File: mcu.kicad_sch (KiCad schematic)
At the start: 23 parts, among them J3 Conn_01x05, J4 Conn_01x05, U13 STM32F405RGTx, Y1 12MHz

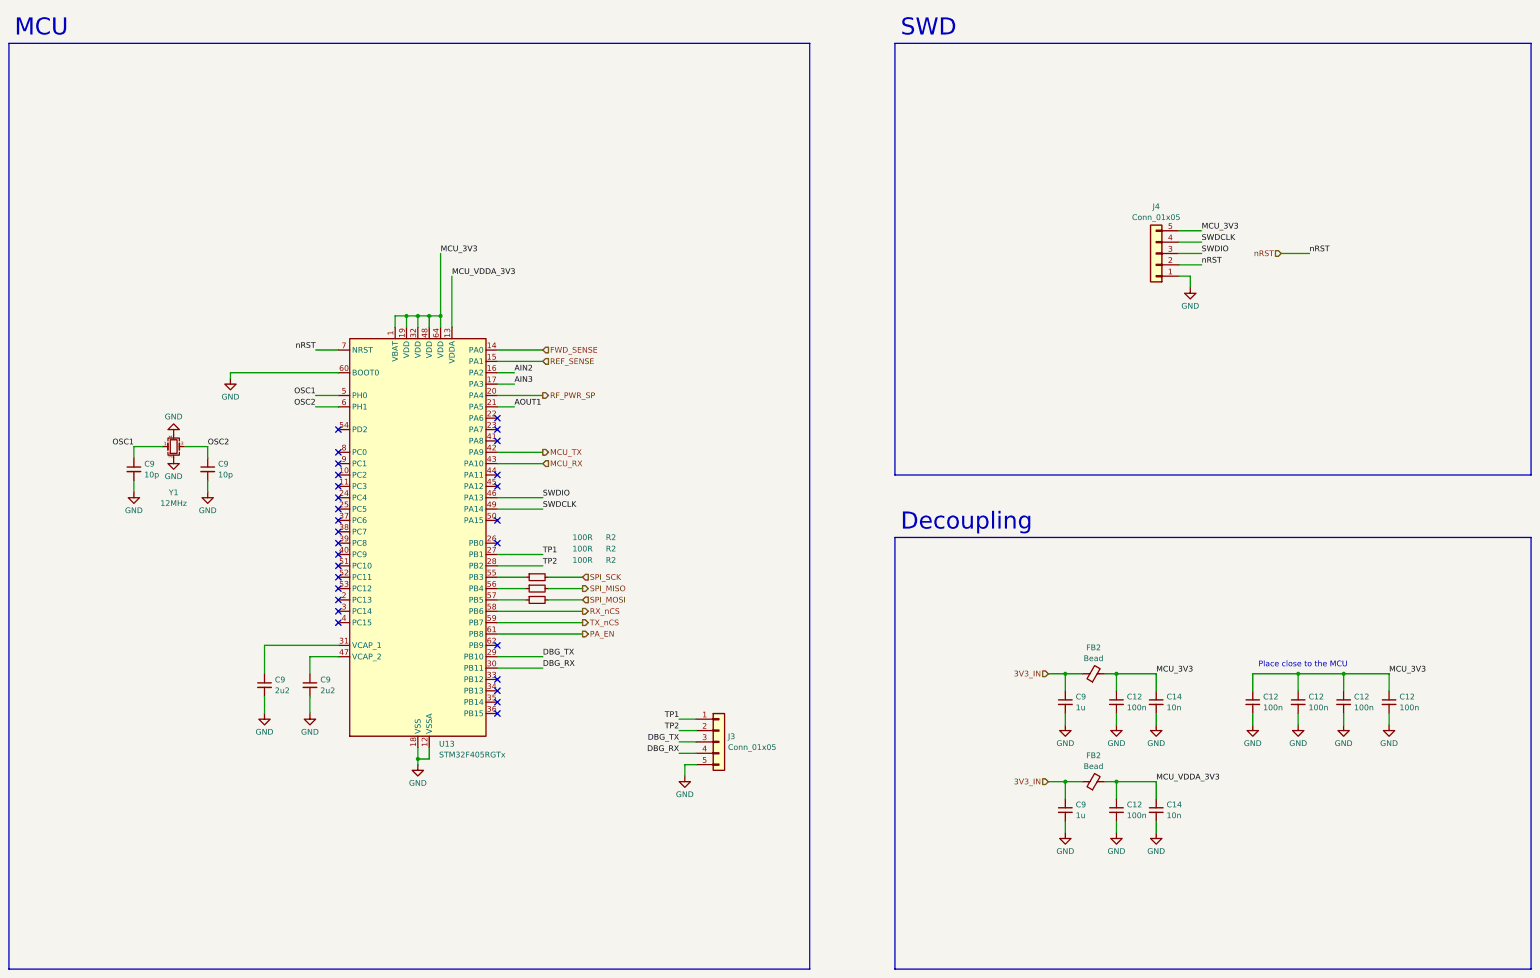
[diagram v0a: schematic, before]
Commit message: significant updates
- supply for the detector block changed from 3.3V to 5V
- minor bugfixes
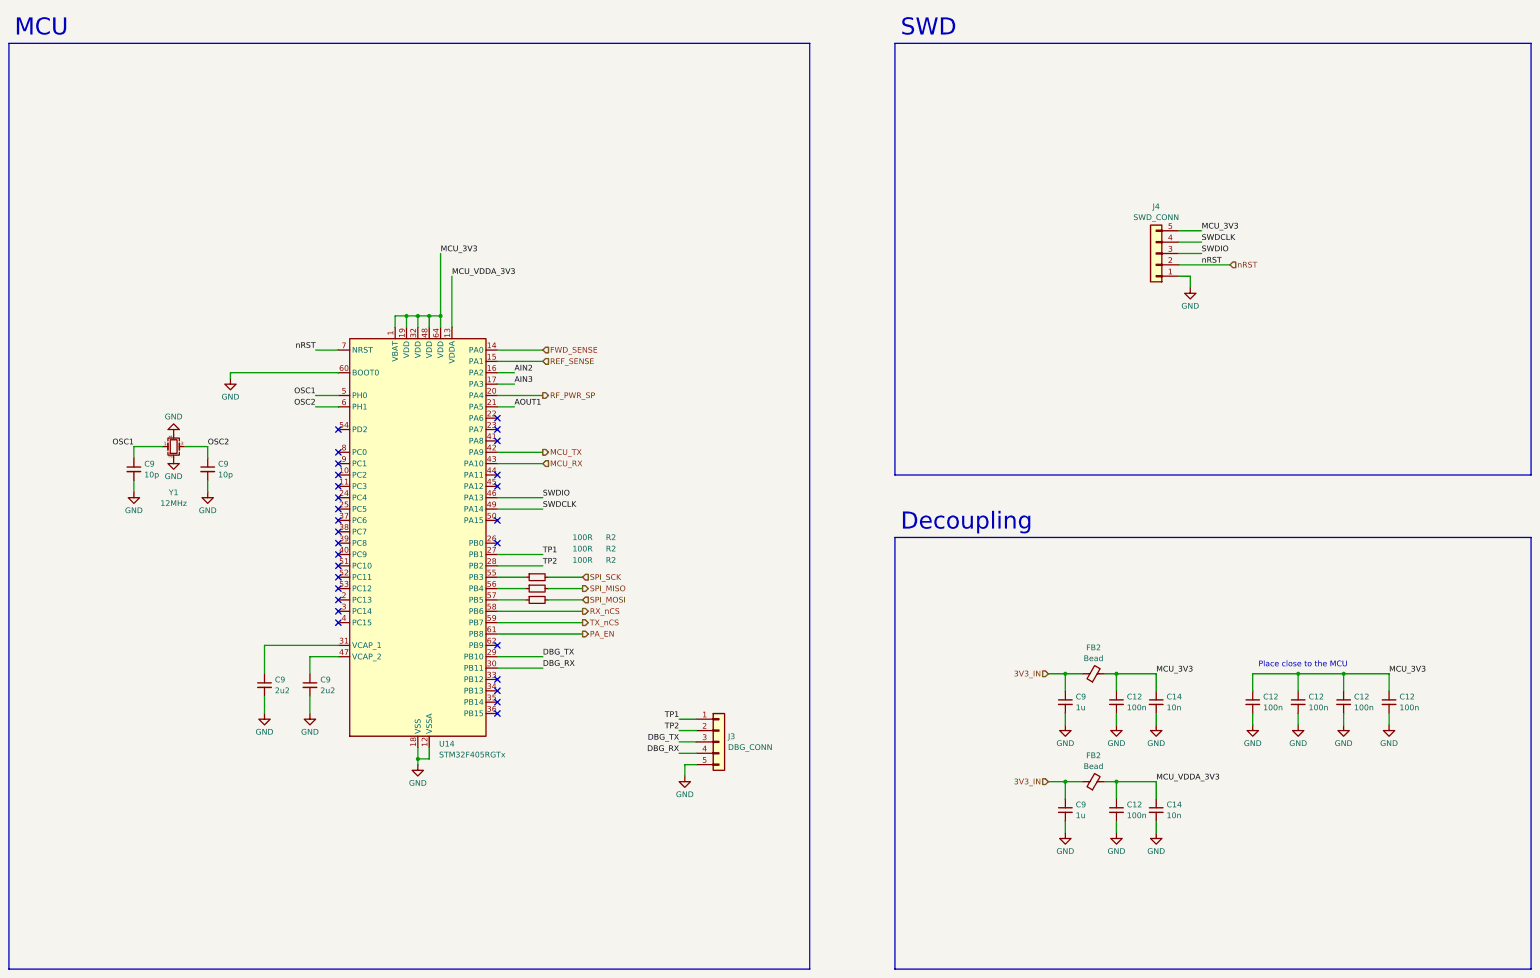
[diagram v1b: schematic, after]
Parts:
- J3: value Conn_01x05 -> DBG_CONN
- J4: value Conn_01x05 -> SWD_CONN
- renumbered U13 to U14

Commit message: PN update
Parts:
- C9: PN (none) -> 06035A100JAT2A
- FB2: PN (none) -> BLM18KG601SH1D
- J3, J4: PN (none) -> TSM-105-01-T-SV-TR
- U14: value STM32F405RGTx -> STM32F405RGT6; PN (none) -> STM32F405RGT6
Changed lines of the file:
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@@
+      (effects (font (size 1.27 1.27)) hide)
+    )
+    (property "PN" "06035A100JAT2A" (at 67.31 134.62 0)
       (effects (font (size 1.27 1.27)) hide)
     )
@@
       (effects (font (size 1.27 1.27)) hide)
     )
-    (property "PN" "" (at 281.94 204.47 90)
+    (property "PN" "BLM18KG601SH1D" (at 281.94 204.47 90)
       (effects (font (size 1.27 1.27)) hide)
     )
@@
       (effects (font (size 1.27 1.27)) hide)
     )
+    (property "PN" "06035A100JAT2A" (at 83.82 134.62 0)
+      (effects (font (size 1.27 1.27)) hide)
+    )
     (pin "1")
     (pin "2")
@@
       (effects (font (size 1.27 1.27)) (justify left))
     )
-    (property "Value" "STM32F405RGTx" (at 135.5441 198.4543 0)
+    (property "Value" "STM32F405RGT6" (at 135.5441 198.4543 0)
       (effects (font (size 1.27 1.27)) (justify left))
     )
@@
     )
     (property "Datasheet" "https://www.st.com/resource/en/datasheet/stm32f405rg.pdf" (at 130.81 151.13 0)
+      (effects (font (size 1.27 1.27)) hide)
+    )
+    (property "PN" "STM32F405RGT6" (at 130.81 151.13 0)
       (effects (font (size 1.27 1.27)) hide)
     )
@@
       (effects (font (size 1.27 1.27)) hide)
     )
+    (property "PN" "TSM-105-01-T-SV-TR" (at 198.12 195.58 0)
+      (effects (font (size 1.27 1.27)) hide)
+    )
     (pin "1")
     (pin "2")
@@
       (effects (font (size 1.27 1.27)) hide)
     )
-    (property "PN" "" (at 281.94 180.34 90)
+    (property "PN" "BLM18KG601SH1D" (at 281.94 180.34 90)
       (effects (font (size 1.27 1.27)) hide)
     )
@@
       (effects (font (size 1.27 1.27)) hide)
     )
+    (property "PN" "TSM-105-01-T-SV-TR" (at 295.91 86.36 0)
+      (effects (font (size 1.27 1.27)) hide)
+    )

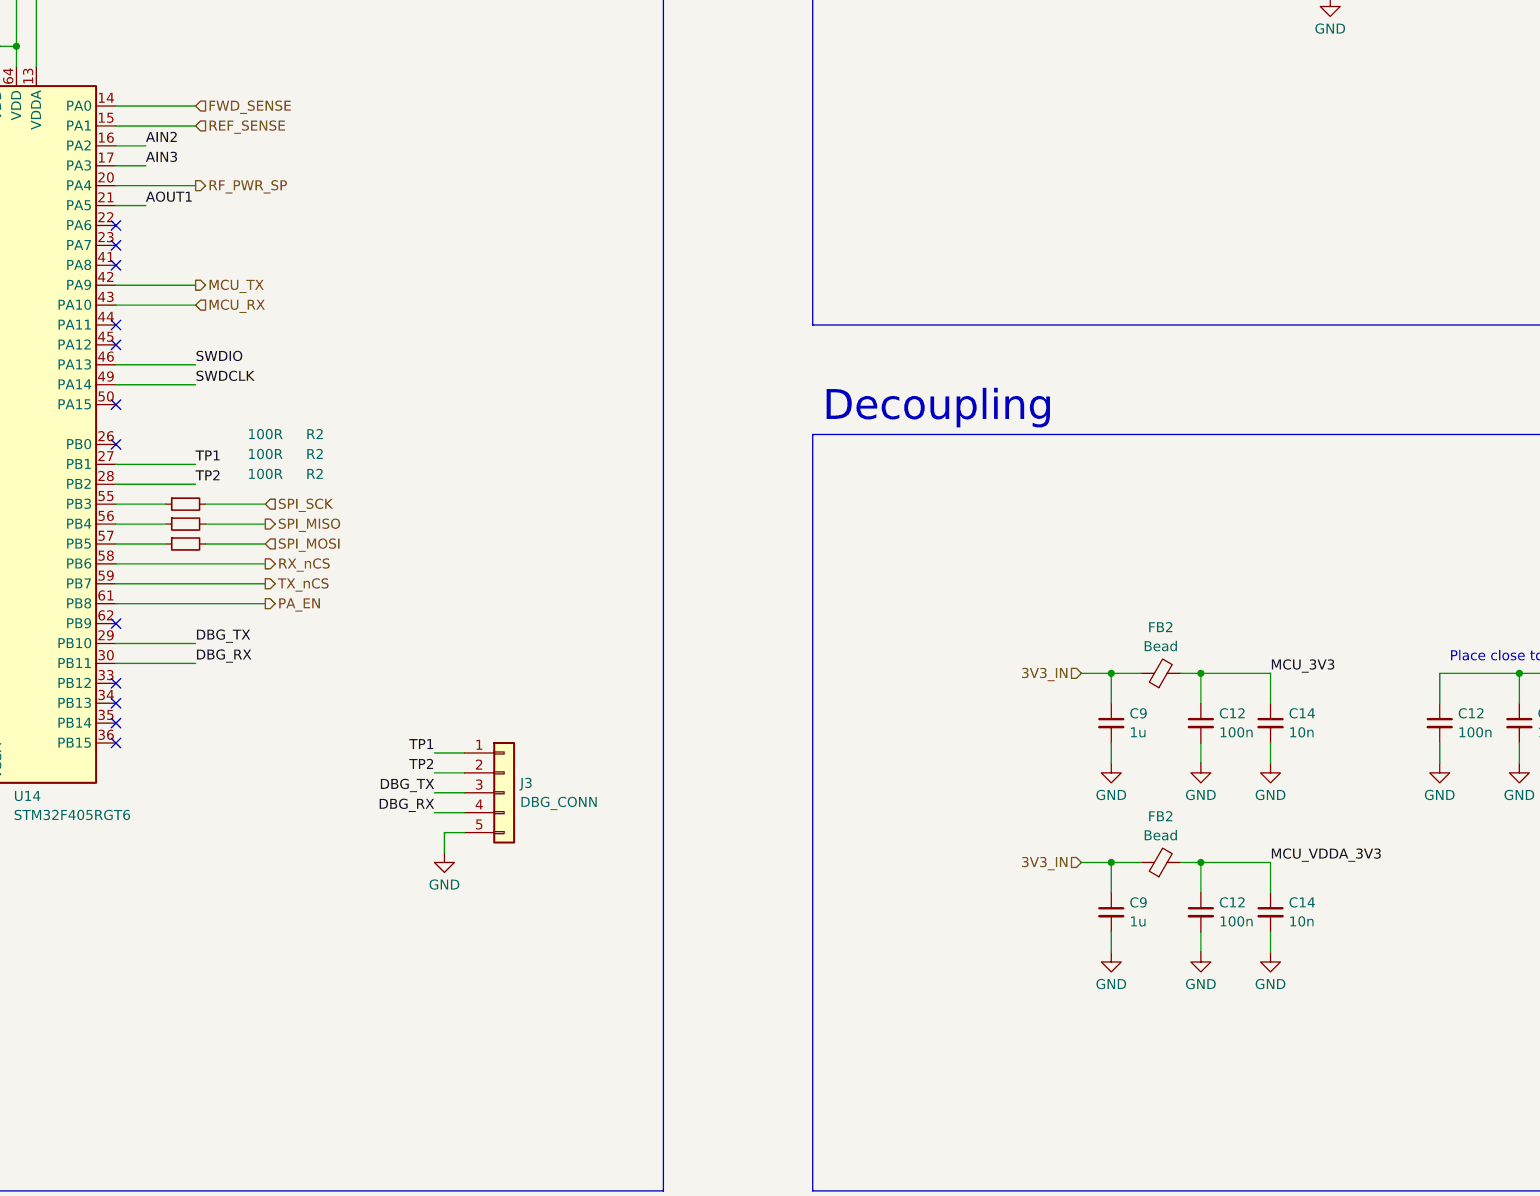
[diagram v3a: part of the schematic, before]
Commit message: `PWR_FLAG`, ERC cleanup
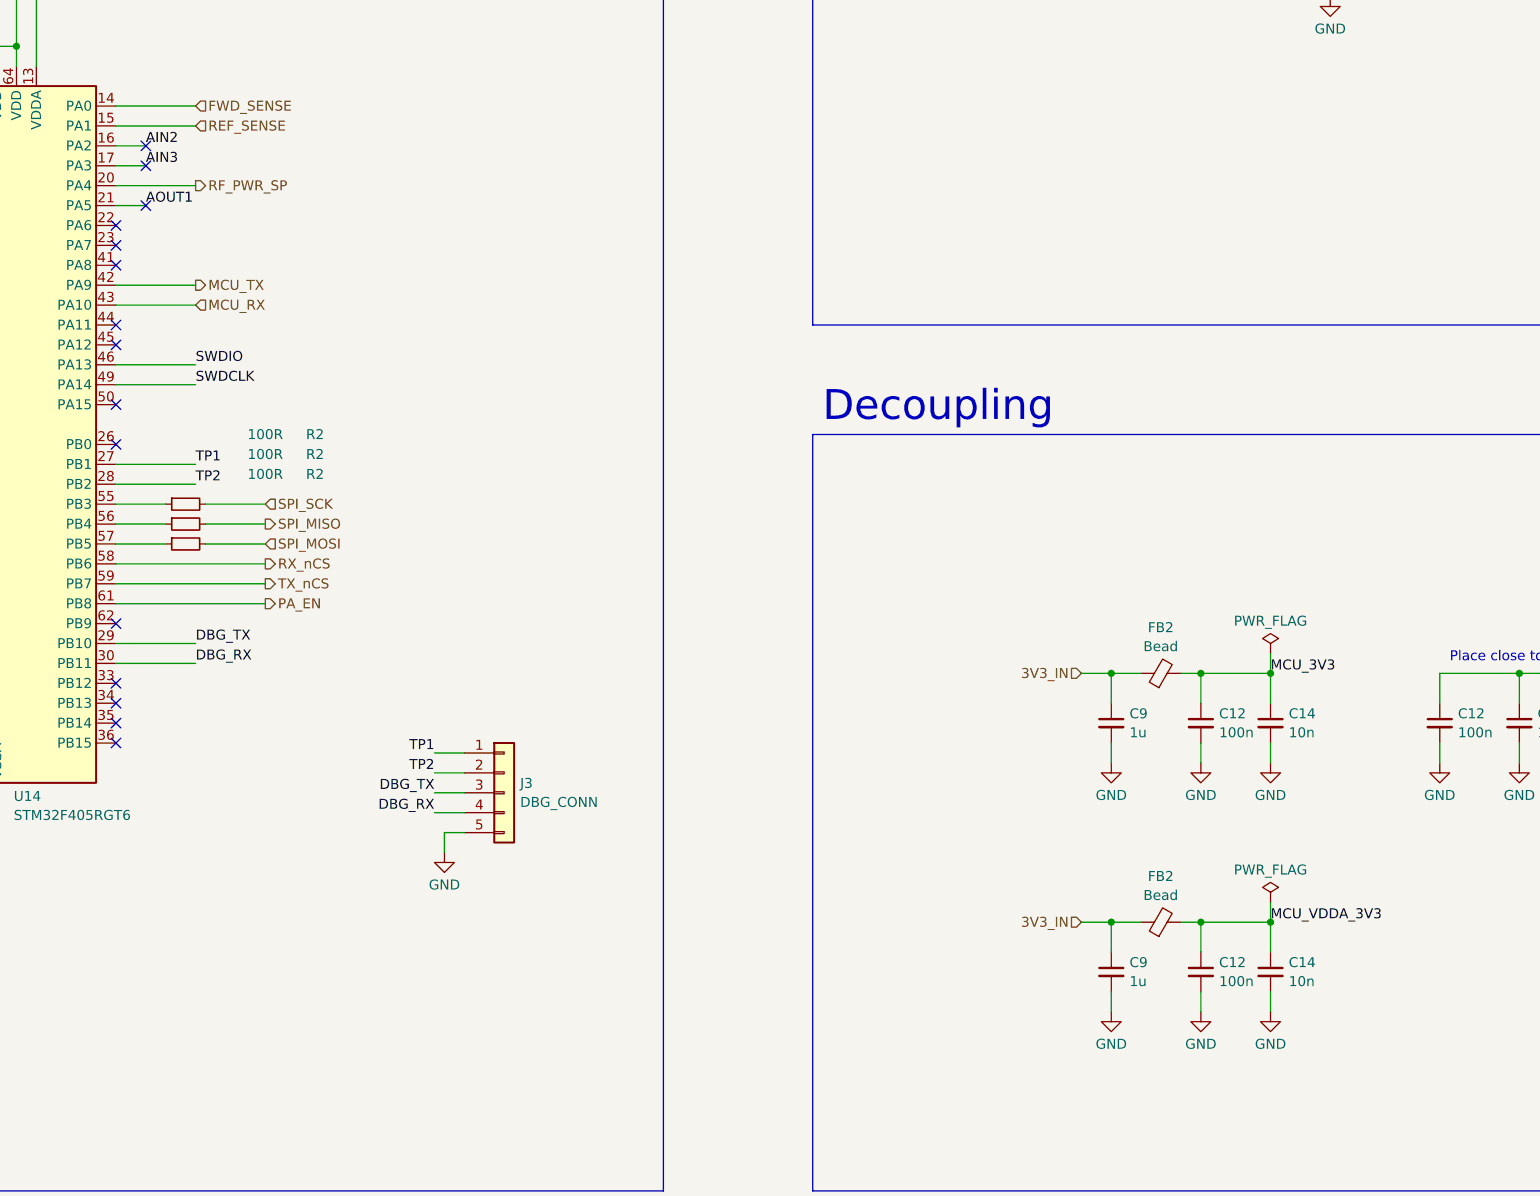
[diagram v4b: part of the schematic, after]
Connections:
- no-connect marks 29 -> 32
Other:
- moved on the sheet: C12, C14, C9, FB2

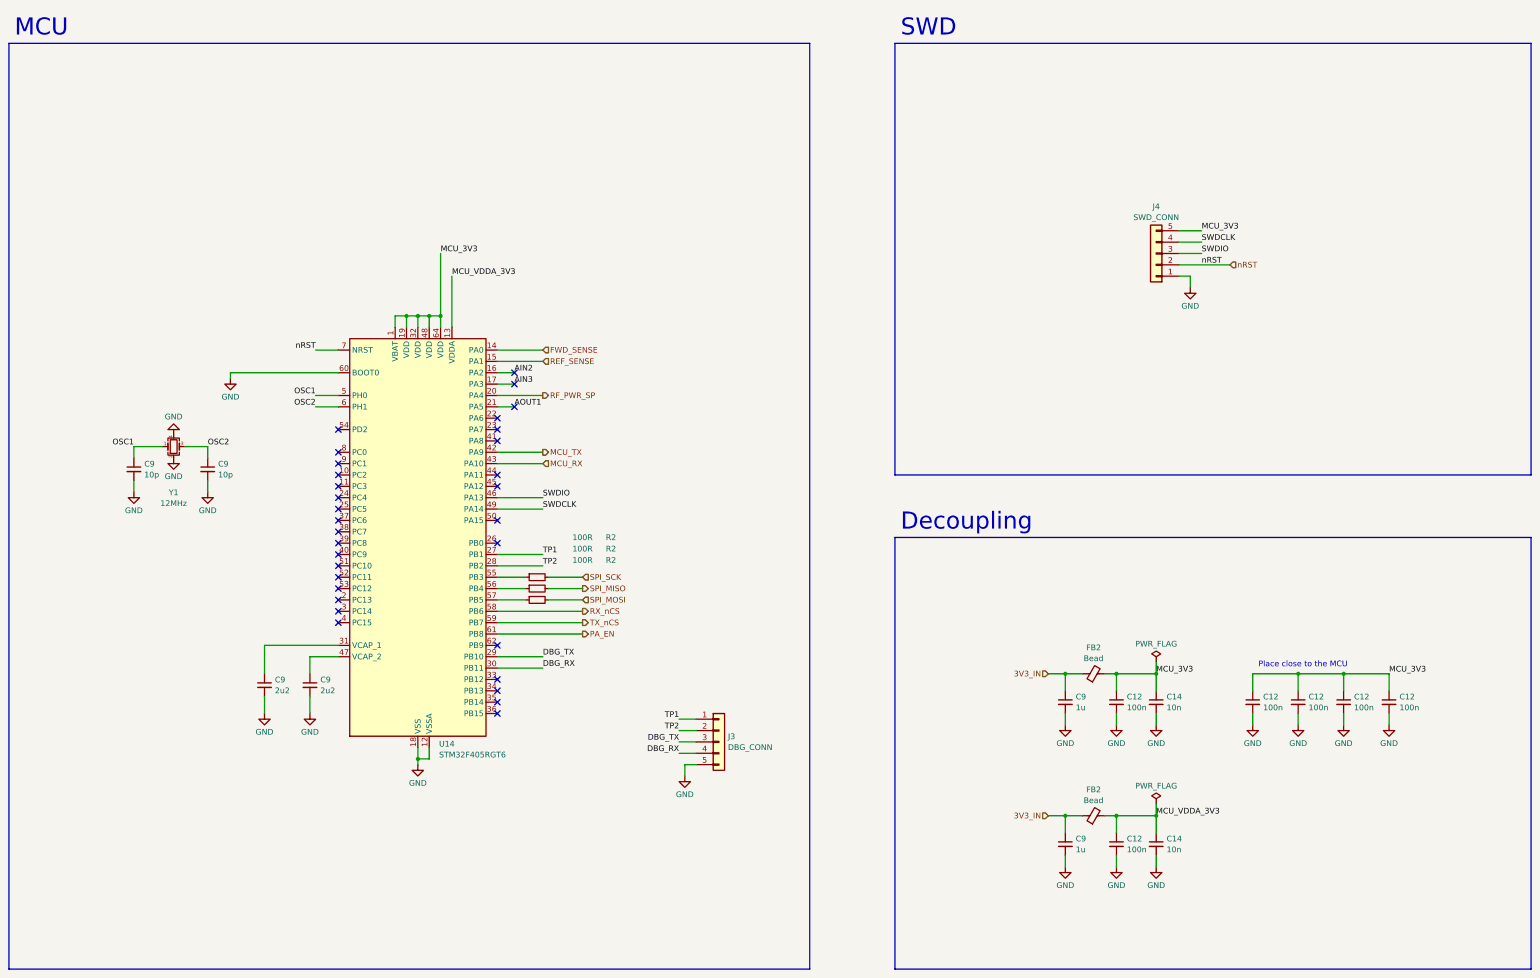
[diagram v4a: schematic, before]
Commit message: TP updates, temp sensor added
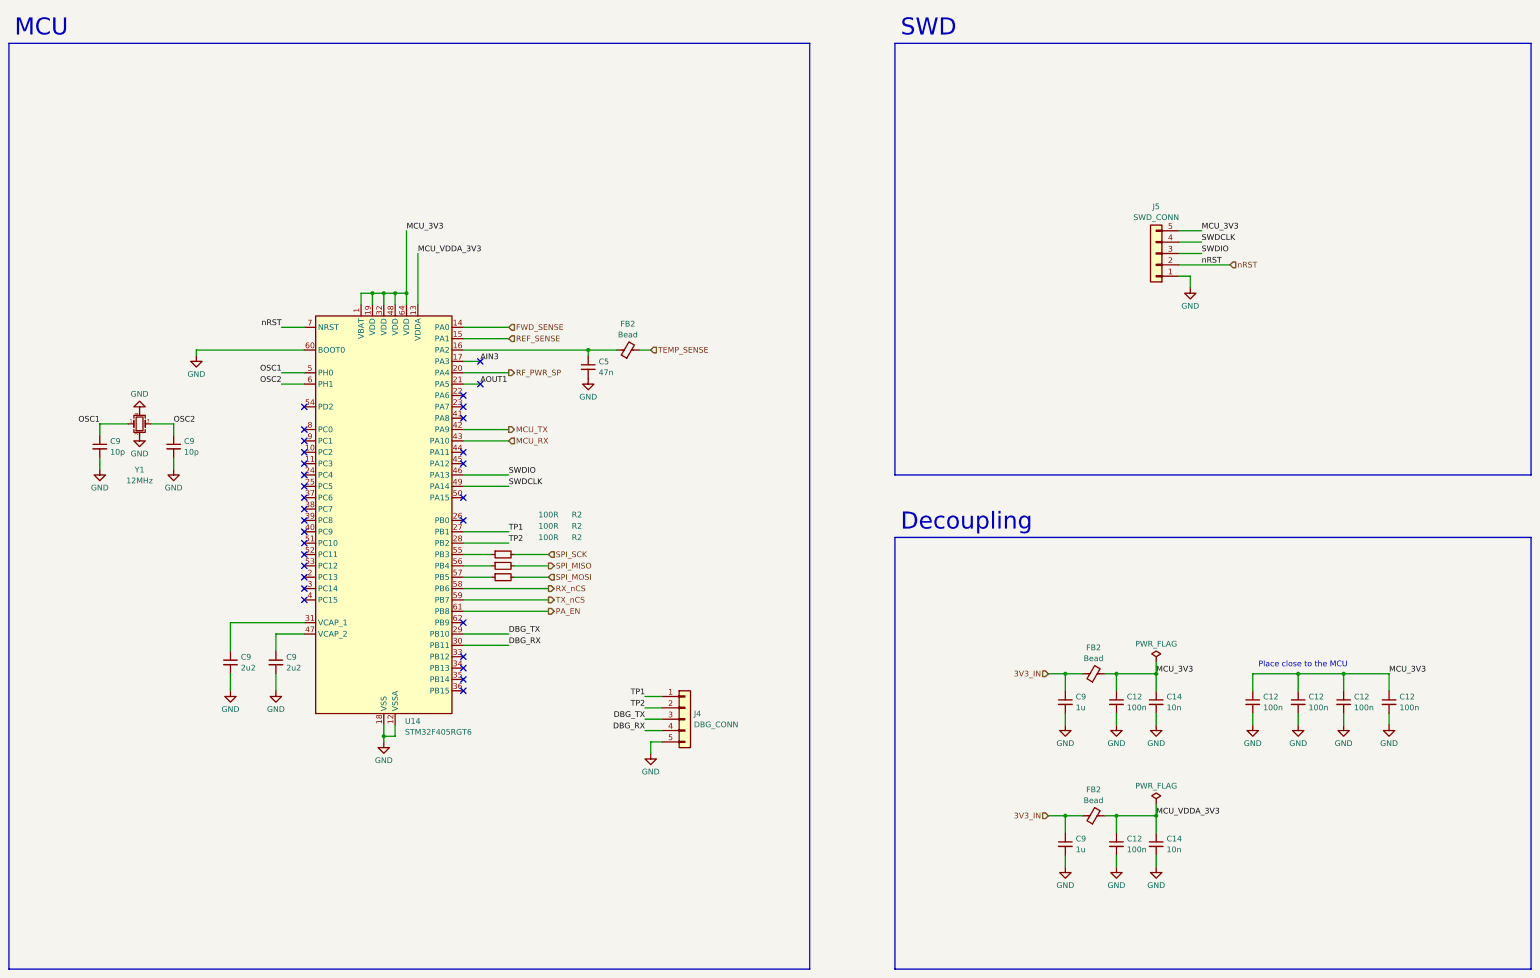
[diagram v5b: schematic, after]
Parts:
- added C5: 47n, Capacitor_SMD:C_0603_1608Metric, symbol Device:C_Small
- added FB2: Bead, Inductor_SMD:L_0603_1608Metric, symbol Device:FerriteBead_Small
- renumbered J3 to J4, J4 to J5
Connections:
- net GND: now also C5.2
- net AIN2: no longer names the net of U14.16 (PA2)
- net AIN2: now also C5.1, FB2.1
- new net TEMP_SENSE: FB2.2
- no-connect marks 32 -> 31
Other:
- moved on the sheet: C9, J4, R2, U14, Y1

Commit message: date update
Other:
- title: M17 Remote Radio Unit - RF board -> Remote Radio Unit - RF board
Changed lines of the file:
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@@
   (paper "A3")
   (title_block
-    (title "M17 Remote Radio Unit - RF board")
-    (date "28-10-2023")
+    (title "Remote Radio Unit - RF board")
+    (date "30-10-2023")
     (rev "A")
     (company "M17 Project")
